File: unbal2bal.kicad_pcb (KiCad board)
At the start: 2 copper layers, 76 x 90 mm, 30 parts, among them J1 901, J2 NMJ6HFD2, J3 Mini-DIN-3, J4 Mini-DIN-4, U1 LM4562

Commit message: update TODO
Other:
- board text added: "TODO - change RCA connector to something without a cursed footprint - testpoints"
- board text removed: "TODO - change RCA connector to something without a cursed footprint - add license, made in kicad decals - add metadata - testpoints"
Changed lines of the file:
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@@
     (effects (font (size 1 1) (thickness 0.15)) (justify left))
   )
-  (gr_text "TODO\n\n- change RCA connector to something without a cursed footprint\n- add license, made in kicad decals\n- add metadata\n- testpoints" (at 218 72) (layer "Cmts.User")
+  (gr_text "TODO\n\n- change RCA connector to something without a cursed footprint\n- testpoints" (at 218 72) (layer "Cmts.User")
     (effects (font (size 1 1) (thickness 0.15)) (justify left))
   )

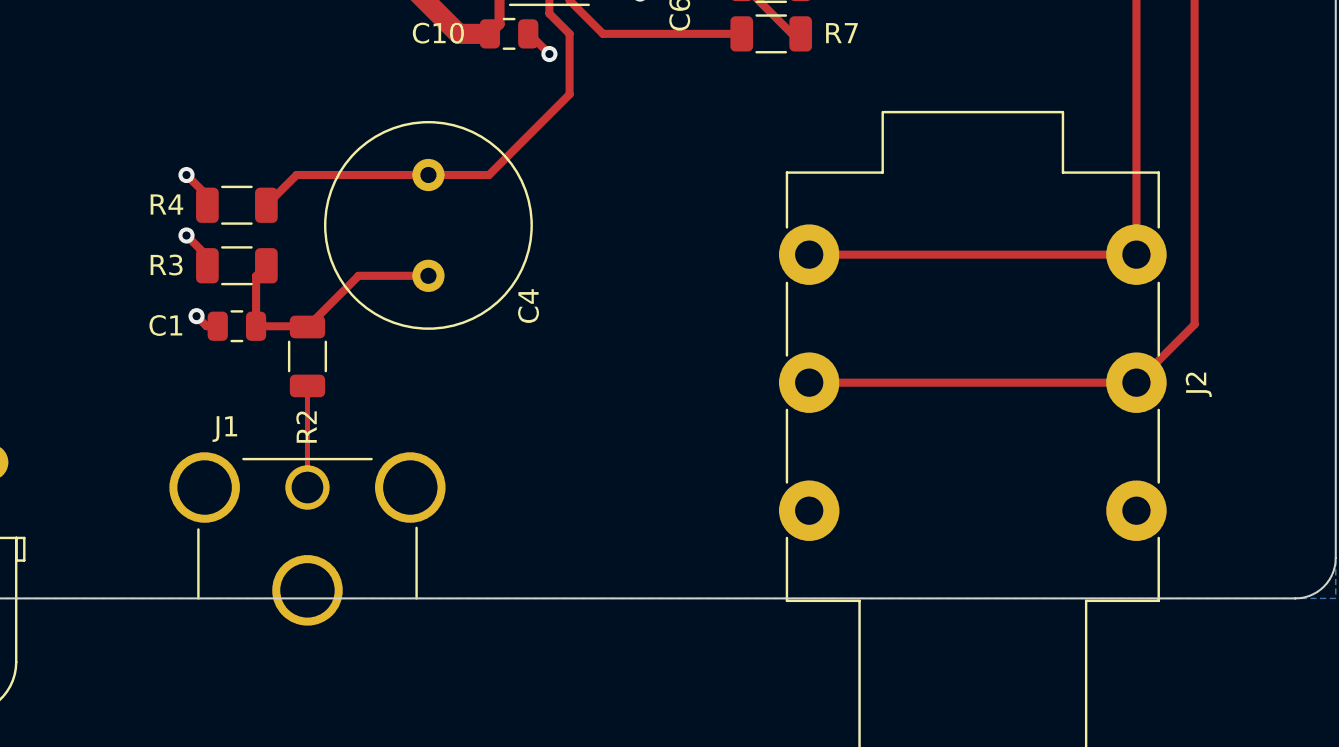
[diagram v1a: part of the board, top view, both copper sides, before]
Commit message: switch RCA jack to a nicer model
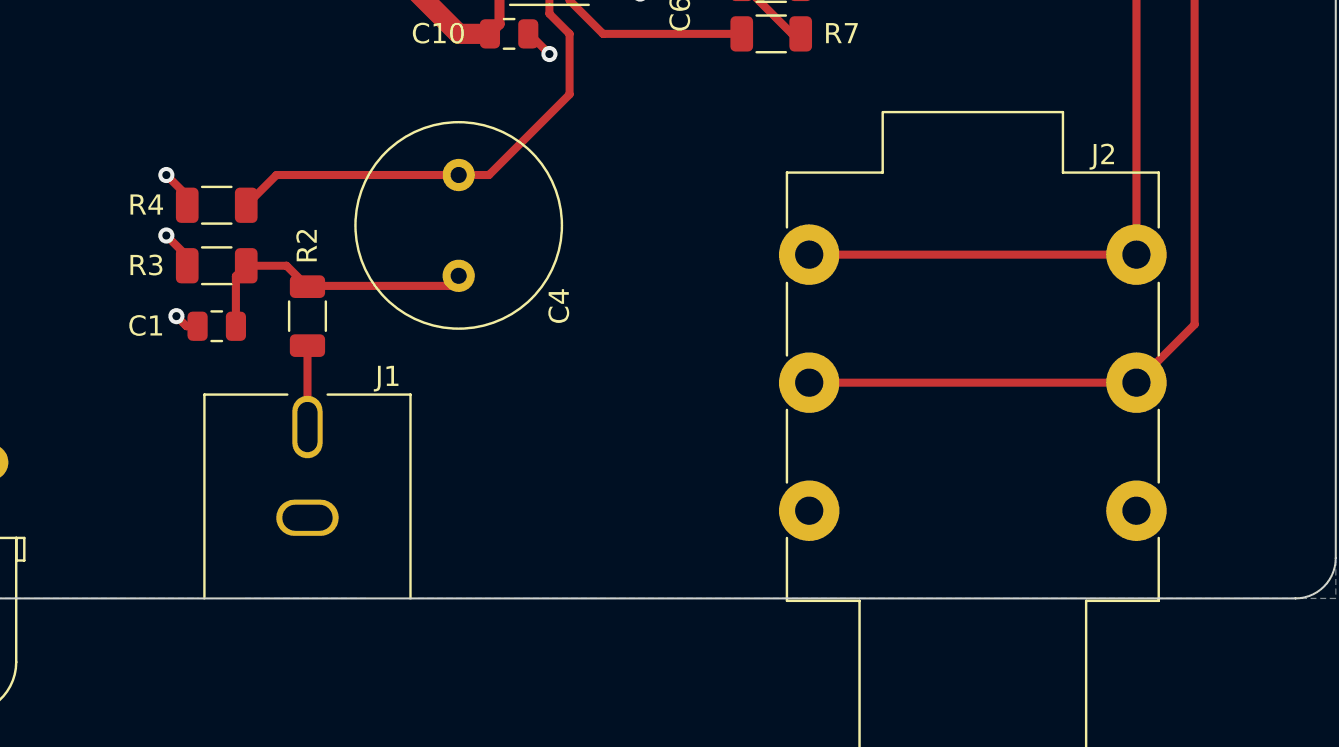
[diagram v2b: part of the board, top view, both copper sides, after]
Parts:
- J1: value 901 -> RCJ-041; footprint Connector_Audio_gkeeth:RCA_Keystone_901_Horizontal -> Connector_Audio_gkeeth:RCA_CUI_RCJ-04x_Horizontal
- moved J1 3.00 mm to (125.0, 141.5)
- moved R2 2.00 mm to (125.0, 136.0)
- moved C4 1.50 mm to (132.5, 134.0)
- moved C1 1.00 mm to (120.5, 136.5)
- moved R3 1.00 mm to (120.5, 133.5)
- moved R4 1.00 mm to (120.5, 130.5)
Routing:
- net Net-(C1-Pad1): track 12.8 -> 14.4 mm
- net Net-(J1-PadT): track 5.04 -> 4.04 mm
- net Net-(C4-Pad2): track 25.8 -> 26.8 mm
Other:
- board text added: "TODO - testpoints"
- board text removed: "TODO - change RCA connector to something without a cursed footprint - testpoints"

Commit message: update TODOs
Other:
- board text added: "TODO - testpoints - think about RCA grounding - check that capacitors fit"
- board text removed: "TODO - testpoints"
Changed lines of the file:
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@@
     (effects (font (size 1 1) (thickness 0.15)) (justify left))
   )
-  (gr_text "TODO\n- testpoints" (at 218 72) (layer "Cmts.User")
+  (gr_text "TODO\n- testpoints\n- think about RCA grounding\n- check that capacitors fit" (at 218 72) (layer "Cmts.User")
     (effects (font (size 1 1) (thickness 0.15)) (justify left))
   )

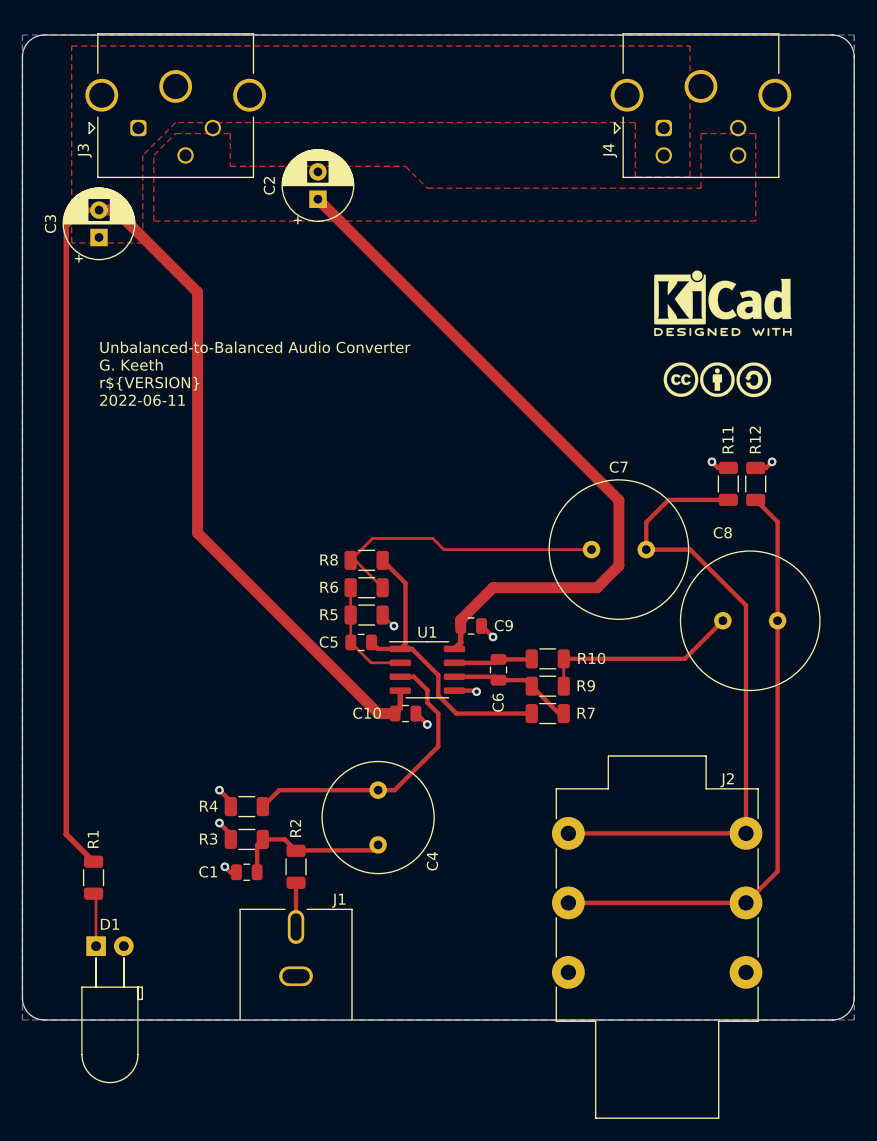
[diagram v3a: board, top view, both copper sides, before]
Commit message: move output coupling caps to horizontal to fit into enclosure
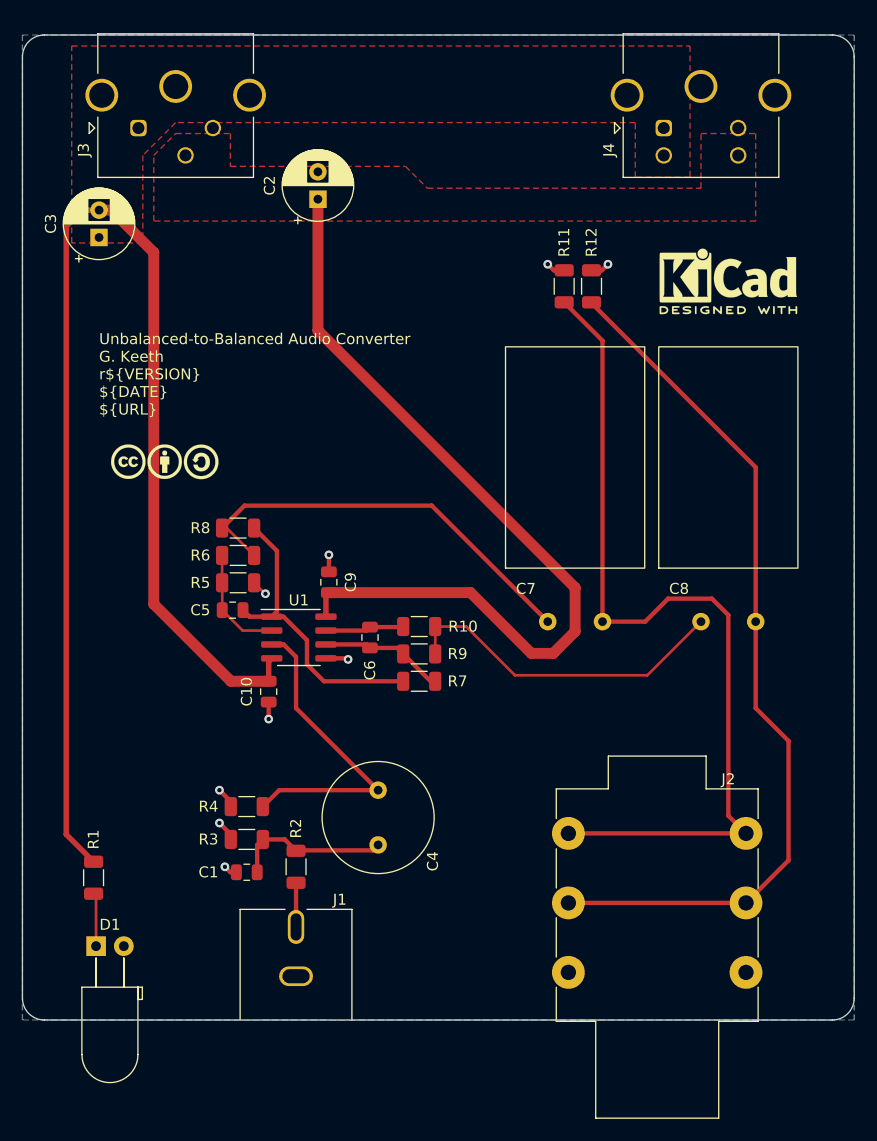
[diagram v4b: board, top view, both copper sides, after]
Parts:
- C7, C8: footprint Capacitor_THT:C_Radial_D12.5mm_H25.0mm_P5.00mm -> Capacitor_THT_gkeeth:C_Radial_D12.5mm_H20.0mm_P5.00mm_Horizontal
- moved LOGO2 51.1 mm to (113.0, 99.0)
- moved R11 23.5 mm to (149.5, 83.0)
- moved R12 23.5 mm to (152.0, 83.0)
- moved C9 13.6 mm to (128.0, 110.0), turned to 90 degrees
- moved C10 12.7 mm to (122.5, 120.0), turned to 90 degrees
- moved C6 12.1 mm to (131.8, 115.0)
- moved R10 12.1 mm to (136.3, 114.0)
- moved R7 12.1 mm to (136.3, 119.0)
- moved R9 12.1 mm to (136.3, 116.5)
- moved U1 12.1 mm to (125.3, 115.0)
- moved C5 12.1 mm to (119.2, 112.5)
- moved R5 12.1 mm to (119.7, 110.0)
- moved R6 12.1 mm to (119.7, 107.5)
- moved R8 12.1 mm to (119.7, 105.0)
- moved C7 7.70 mm to (148.0, 113.6)
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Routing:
- net Net-(C8-Pad2): track 55.1 -> 80.2 mm
- net Net-(C7-Pad2): track 59.1 -> 80.5 mm
- net VCC: track 64.3 -> 77.2 mm
- net Net-(C8-Pad1): track 18.5 -> 30.7 mm
- net Net-(C7-Pad1): track 27.2 -> 39.0 mm
- net VEE: track 124.0 -> 117.1 mm
- net Net-(C4-Pad2): track 26.8 -> 29.1 mm
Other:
- board text added: "TODO - testpoints - think about RCA grounding"
- board text added: "Unbalanced-to-Balanced Audio Converter G. Keeth r${VERSION} ${DATE} ${URL}"
- board text removed: "TODO - testpoints - think about RCA grounding - check that capacitors fit"
- board text removed: "Unbalanced-to-Balanced Audio Converter G. Keeth r${VERSION} 2022-06-11"

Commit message: minor updates, labels, etc
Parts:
- added TP1: TestPoint_2Pole, Connector_PinHeader_2.54mm:PinHeader_1x02_P2.54mm_Vertical, F.Cu at (137.0, 71.0)
- added TP2: TestPoint_2Pole, Connector_PinHeader_2.54mm:PinHeader_1x02_P2.54mm_Vertical, F.Cu at (147.0, 69.0)
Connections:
- net Net-(C7-Pad2) renamed /hot_out
- net Net-(C8-Pad2) renamed /cold_out
- net Net-(J1-PadT) renamed /unbal_in
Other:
- board text added: "JLCJLCJLCJLC"
- board text added: "TODO - think about RCA grounding"
- board text removed: "TODO - testpoints - think about RCA grounding"

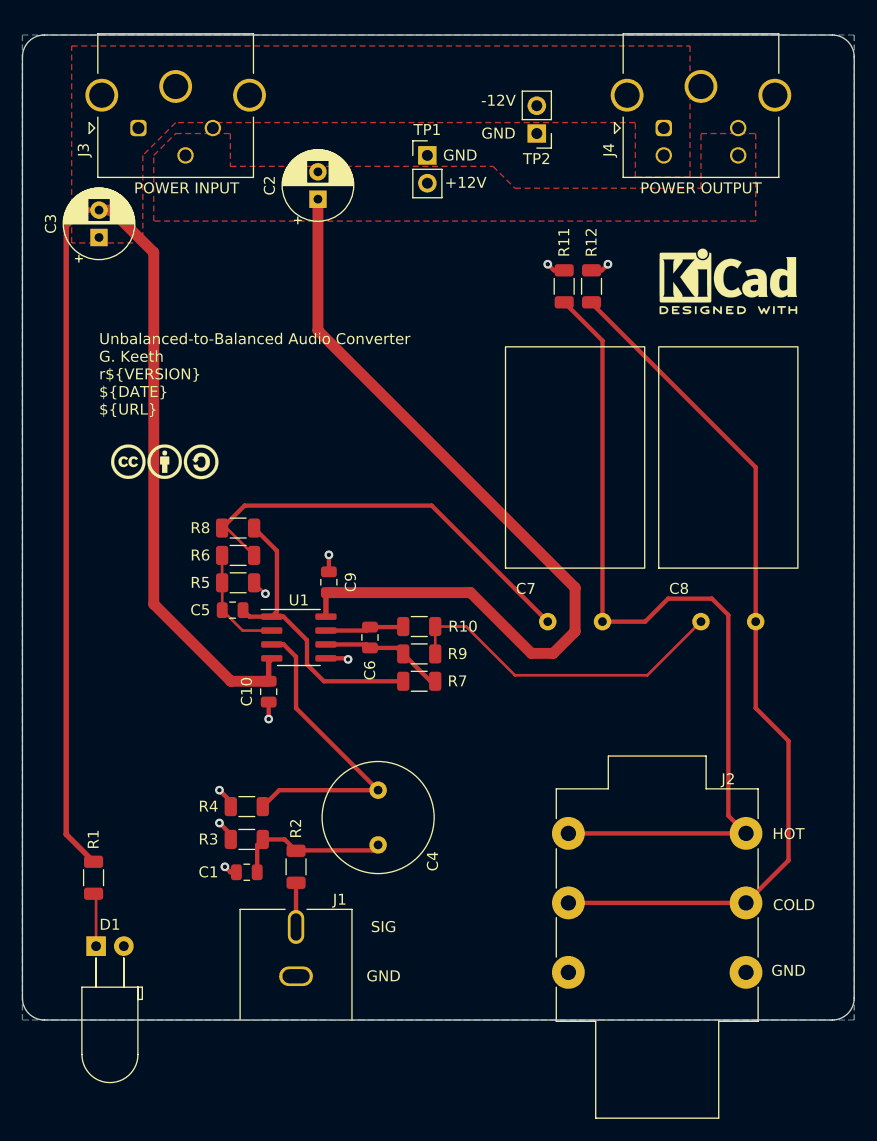
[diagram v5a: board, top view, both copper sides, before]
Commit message: update grounding
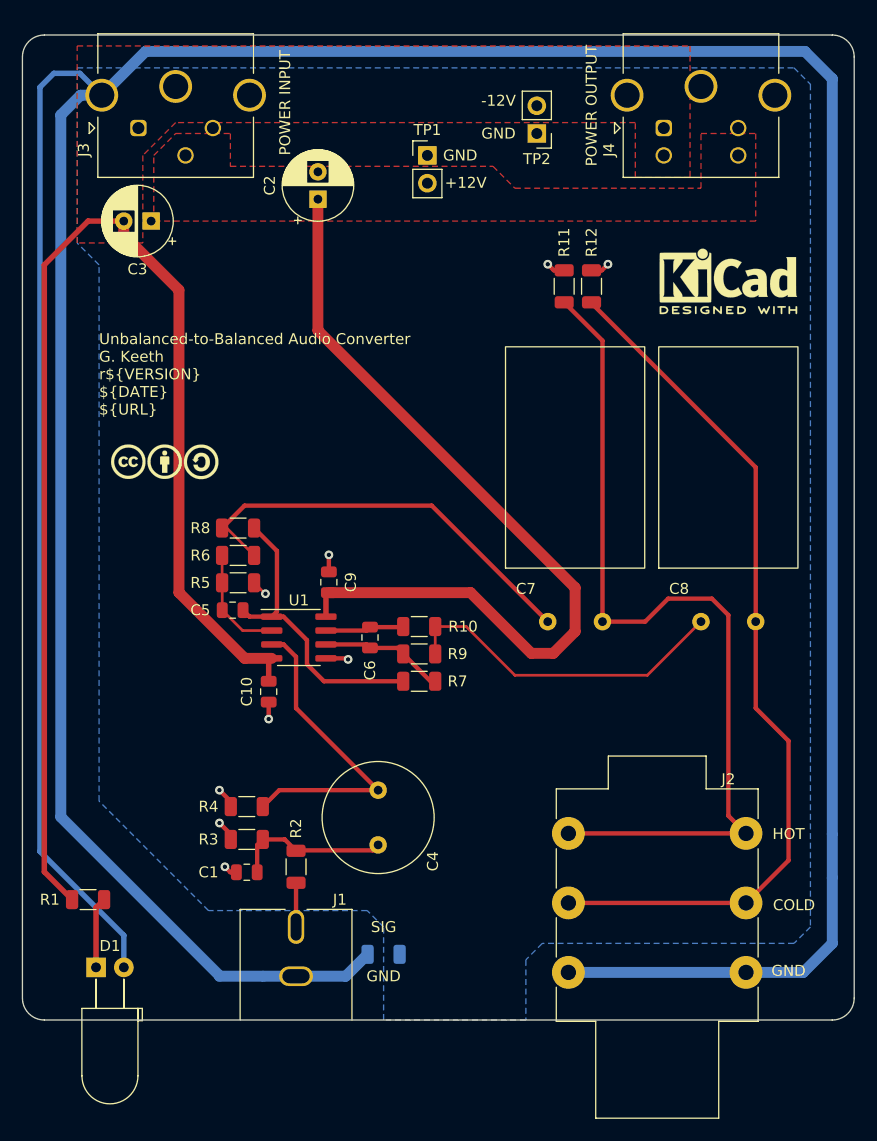
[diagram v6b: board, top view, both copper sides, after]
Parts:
- added NT1: NetTie_2, Net_Tie_gkeeth:NetTie-2_SMD_Pad1.0mm, B.Cu at (120.0, 146.0)
- added NT2: NetTie_2, Net_Tie_gkeeth:NetTie-2_SMD_Pad1.0mm, B.Cu at (174.0, 135.0)
- added R13: 0 DNP, Resistor_SMD:R_1206_3216Metric, B.Cu at (133.0, 144.0)
- moved C3 4.99 mm to (111.8, 77.0), turned to 180 degrees
- moved R1 2.06 mm to (106.0, 139.0), turned to 180 degrees
- moved D1 1.94 mm to (106.7, 145.2)
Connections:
- J1 pad S: GND -> Net-(J1-PadS)
- J2 pad S: GND -> Net-(J2-PadS)
- J2 pad SN: GND -> Net-(J2-PadS)
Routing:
- net GND: track 15.2 -> 333.4 mm
- net Net-(J2-PadS): track 0.00 -> 31.2 mm
- net Net-(J1-PadS): track 0.00 -> 10.4 mm
- net Net-(D1-Pad1): track 4.88 -> 6.50 mm
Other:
- board text added: "DNP TO USE STAR GROUND"
- board text removed: "TODO - think about RCA grounding"

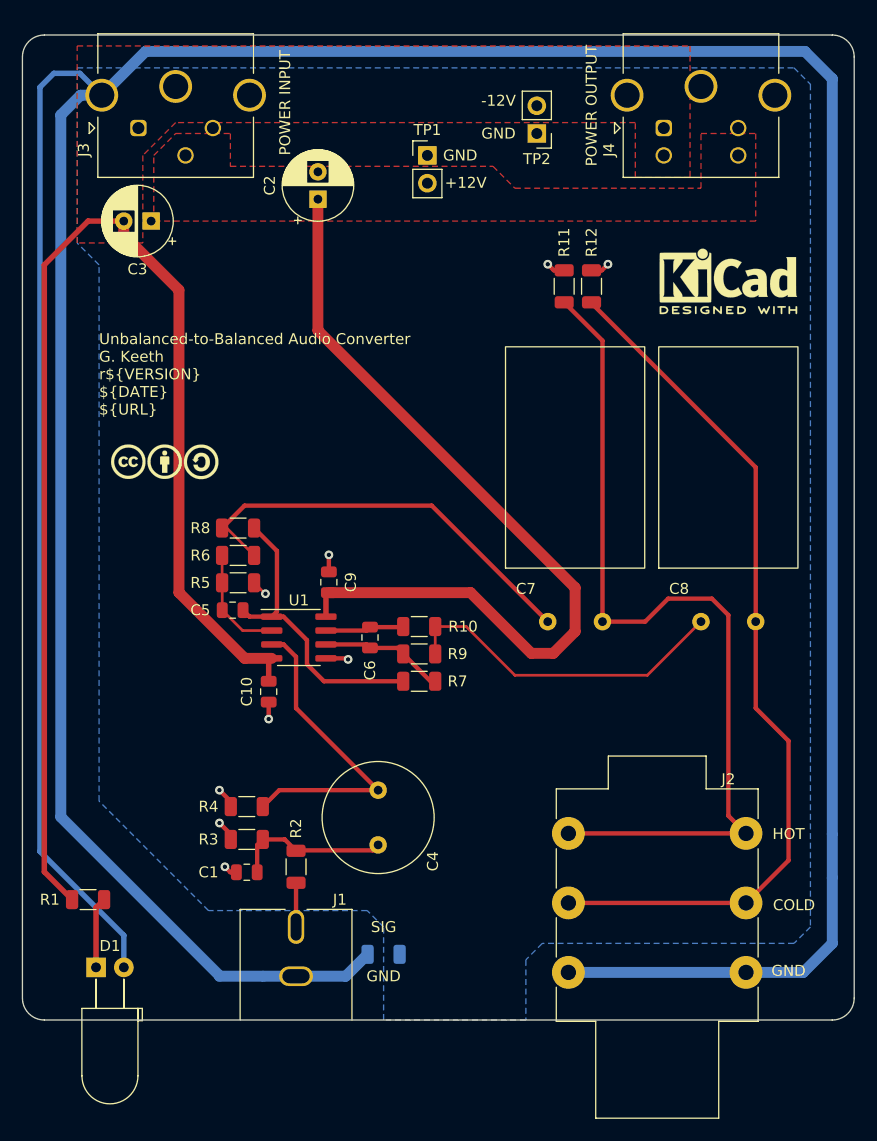
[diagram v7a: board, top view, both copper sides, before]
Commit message: change to lower profile 1/4in jack
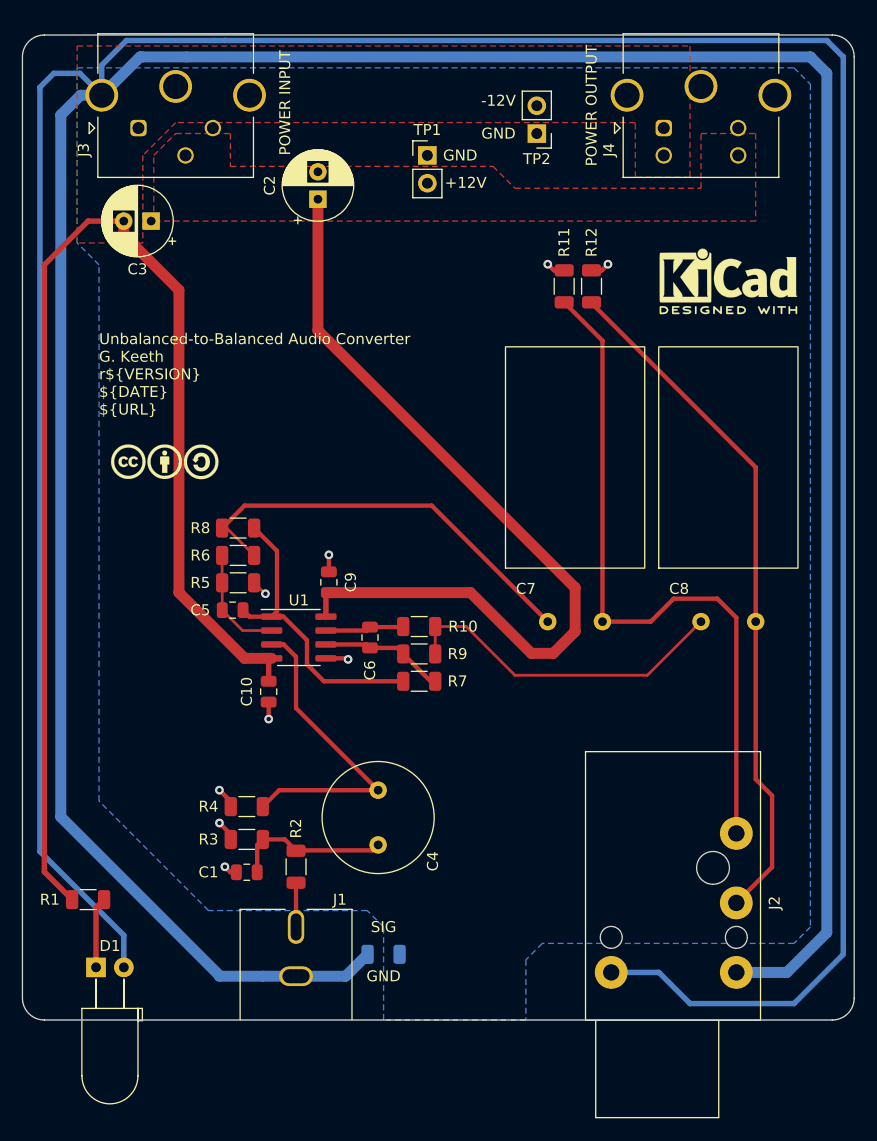
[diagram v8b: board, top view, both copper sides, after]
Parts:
- added NT3: NetTie_2, NetTie:NetTie-2_SMD_Pad0.5mm, B.Cu at (118.0, 60.5)
- J2: value NMJ6HFD2 -> NRJ3HF-1; footprint Connector_Audio:Jack_6.35mm_Neutrik_NMJ6HFD2_Horizontal -> Connector_Audio:Jack_6.35mm_Neutrik_NRJ3HF-1_Horizontal
- moved NT2 95.1 mm to (113.0, 62.0), turned to 180 degrees
- moved J2 0.89 mm to (165.2, 132.9)
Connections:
- J2 pad S: Net-(J2-PadS) -> Net-(NT2-Pad1)
- NT2 pad 1: Net-(J2-PadS) -> Net-(NT2-Pad1)
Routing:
- net Net-(J2-PadG): track 0.00 -> 163.4 mm
- net Net-(NT2-Pad1): track 0.00 -> 147.4 mm
- net GND: track 333.4 -> 214.1 mm
- net Net-(J2-PadS): track 31.2 -> 0.00 mm
- net /cold_out: track 80.2 -> 63.1 mm
- net /hot_out: track 80.5 -> 64.2 mm
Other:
- board text added: "TODO 3d model for NRJ3HF-1 add front panel grounding ring to 1/4{dblquote} jack front panel? Double check horizontal position of 1/4{dblquote} jack"
